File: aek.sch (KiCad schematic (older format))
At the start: 223 parts, among them J1 Conn_01x04_MountingPin, SW1 SW_Push, U1 ATmega32U4-AU, Y1 16MHz

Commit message: updates
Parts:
- added H1, H2: MountingHole_Pad, MountingHole:MountingHole_2.7mm_M2.5_Pad, symbol Mechanical:MountingHole_Pad
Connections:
- net GND: now also H1.1, H2.1

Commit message: first draft
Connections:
- net COL0: now also U1.32 (PC7); no longer U1.19 (PD1)
- net COL1: now also U1.31 (PC6); no longer U1.20 (PD2)
- net COL2: now also U1.30 (PB6); no longer U1.21 (PD3)
- net COL3: now also U1.29 (PB5); no longer U1.25 (PD4)
- net COL4: now also U1.28 (PB4); no longer U1.22 (PD5)
- net COL5: now also U1.27 (PD7); no longer U1.26 (PD6)
- net COL6: now also U1.26 (PD6); no longer U1.27 (PD7)
- net COL7: now also U1.25 (PD4); no longer U1.41 (PF0)
- net COL8: now also U1.21 (PD3); no longer U1.40 (PF1)
- net COL9: now also U1.8 (PB0); no longer U1.39 (PF4)
- net ROW0: now also U1.22 (PD5); no longer D100.1 (K), U1.8 (PB0)
- net ROW1: now also U1.37 (PF6); no longer U1.9 (PB1)
- net ROW10: now also D100.1 (K), U1.38 (PF5); no longer D110.1 (K), U1.18 (PD0)
- net ROW2: now also U1.9 (PB1); no longer U1.10 (PB2)
- net ROW3: now also D103.1 (K), D15.1 (K), D26.1 (K), D37.1 (K), D4.1 (K), D48.1 (K), D59.1 (K), D70.1 (K), D81.1 (K), D92.1 (K)
- net ROW4: now also U1.18 (PD0); no longer U1.28 (PB4)
- net ROW5: now also U1.20 (PD2); no longer U1.29 (PB5)
- net ROW6: now also U1.19 (PD1); no longer U1.30 (PB6)
- net ROW8: now also D109.1 (K), U1.10 (PB2); no longer U1.31 (PC6)
- net ROW9: now also D110.1 (K), U1.36 (PF7); no longer D109.1 (K), U1.32 (PC7)
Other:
- moved on the sheet: D100, D109, D110, SW_KPASTR1, SW_KPMINUS1, SW_POW1
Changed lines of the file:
@@
 Wire Wire Line
 	8200 7500 8200 9000
-Connection ~ 12350 1500
 Connection ~ 11650 1500
 Connection ~ 10950 1500
@@
 Connection ~ 6850 1500
 Wire Wire Line
-	12350 1500 12350 1150
-Wire Wire Line
-	12350 1500 12350 2250
-Wire Wire Line
 	11650 1500 11650 1150
 Wire Wire Line
@@
 ROW0
 Wire Wire Line
-	12050 9200 12150 9200
+	12050 8450 12150 8450
 $Comp
 L Device:D_Small D110
 U 1 1 6145A318
-P 12050 9300
-F 0 "D110" V 12096 9230 50  0000 R CNN
-F 1 "D_Small" V 12005 9230 50  0000 R CNN
-F 2 "Diode_SMD:D_SOD-123" V 12050 9300 50  0001 C CNN
-F 3 "~" V 12050 9300 50  0001 C CNN
-	1    12050 9300
+P 12050 8550
+F 0 "D110" V 12096 8480 50  0000 R CNN
+F 1 "D_Small" V 12005 8480 50  0000 R CNN
+F 2 "Diode_SMD:D_SOD-123" V 12050 8550 50  0001 C CNN
+F 3 "~" V 12050 8550 50  0001 C CNN
+	1    12050 8550
 	0    -1   -1   0
 $EndComp
@@
 Wire Wire Line
 	10650 9400 11350 9400
-Connection ~ 11350 9400
 Wire Wire Line
-	11350 9400 12050 9400
+	11350 8650 12050 8650
 Connection ~ 8600 9400
 Connection ~ 7200 9400
@@
 Wire Wire Line
 	11650 9000 11650 8250
-Wire Wire Line
-	12350 8250 12350 9000
 Connection ~ 6150 8250
 Connection ~ 6850 8250
@@
 Connection ~ 10950 8250
 Connection ~ 11650 8250
-Connection ~ 12350 8250
-Wire Wire Line
-	11350 1900 12050 1900
 Wire Wire Line
 	11350 2650 12050 2650
@@
 	11350 4900 12050 4900
 Wire Wire Line
-	11350 8650 12050 8650
-Connection ~ 11350 8650
+	11350 7900 12050 7900
 Connection ~ 11350 4900
 Connection ~ 11350 4150
 Connection ~ 11350 3400
 Connection ~ 11350 2650
-Connection ~ 11350 1900
 Wire Wire Line
 	6850 2250 6850 3000
@@
 L Device:D_Small D109
 U 1 1 6145A285
-P 12050 8550
-F 0 "D109" V 12096 8480 50  0000 R CNN
-F 1 "D_Small" V 12005 8480 50  0000 R CNN
-F 2 "Diode_SMD:D_SOD-123" V 12050 8550 50  0001 C CNN
-F 3 "~" V 12050 8550 50  0001 C CNN
-	1    12050 8550
+P 12050 7800
+F 0 "D109" V 12096 7730 50  0000 R CNN
+F 1 "D_Small" V 12005 7730 50  0000 R CNN
+F 2 "Diode_SMD:D_SOD-123" V 12050 7800 50  0001 C CNN
+F 3 "~" V 12050 7800 50  0001 C CNN
+	1    12050 7800
 	0    -1   -1   0
 $EndComp
 Wire Wire Line
-	12050 8450 12150 8450
+	12050 7700 12150 7700
 Wire Wire Line
 	7900 7700 8000 7700
@@
 Wire Wire Line
 	11350 1700 11450 1700
-$Comp
-L MX_Alps_Hybrid:MX-NoLED SW_POW1
-U 1 1 6126A487
-P 12200 1550
-F 0 "SW_POW1" H 12233 1773 60  0000 C CNN
-F 1 "MX-NoLED" H 12233 1699 20  0000 C CNN
-F 2 "MX_Alps_Hybrid:MX-1U-NoLED" H 11575 1525 60  0001 C CNN
-F 3 "" H 11575 1525 60  0001 C CNN
-	1    12200 1550
-	1    0    0    -1
-$EndComp
-$Comp
-L Device:D_Small D100
-U 1 1 6126A48D
-P 12050 1800
-F 0 "D100" V 12096 1730 50  0000 R CNN
-F 1 "D_Small" V 12005 1730 50  0000 R CNN
-F 2 "Diode_SMD:D_SOD-123" V 12050 1800 50  0001 C CNN
-F 3 "~" V 12050 1800 50  0001 C CNN
-	1    12050 1800
-	0    -1   -1   0
-$EndComp
-Wire Wire Line
-	12050 1700 12150 1700
 Wire Wire Line
 	1200 8750 1200 8950
@@
 L MX_Alps_Hybrid:MX-NoLED SW_KPASTR1
 U 1 1 6145A31E
-P 12200 9050
-F 0 "SW_KPASTR1" H 12233 9273 60  0000 C CNN
-F 1 "MX-NoLED" H 12233 9199 20  0000 C CNN
-F 2 "MX_Alps_Hybrid:MX-1U-NoLED" H 11575 9025 60  0001 C CNN
-F 3 "" H 11575 9025 60  0001 C CNN
-	1    12200 9050
+P 12200 8300
+F 0 "SW_KPASTR1" H 12233 8523 60  0000 C CNN
+F 1 "MX-NoLED" H 12233 8449 20  0000 C CNN
+F 2 "MX_Alps_Hybrid:MX-1U-NoLED" H 11575 8275 60  0001 C CNN
+F 3 "" H 11575 8275 60  0001 C CNN
+	1    12200 8300
 	1    0    0    -1
 $EndComp
 Wire Wire Line
-	12350 4500 12350 8250
+	12350 4500 12350 7500
 $Comp
 L MX_Alps_Hybrid:MX-NoLED SW_KPMINUS1
 U 1 1 6145A28B
-P 12200 8300
-F 0 "SW_KPMINUS1" H 12233 8523 60  0000 C CNN
-F 1 "MX-NoLED" H 12233 8449 20  0000 C CNN
-F 2 "MX_Alps_Hybrid:MX-1U-NoLED" H 11575 8275 60  0001 C CNN
-F 3 "" H 11575 8275 60  0001 C CNN
-	1    12200 8300
+P 12200 7550
+F 0 "SW_KPMINUS1" H 12233 7773 60  0000 C CNN
+F 1 "MX-NoLED" H 12233 7699 20  0000 C CNN
+F 2 "MX_Alps_Hybrid:MX-1U-NoLED" H 11575 7525 60  0001 C CNN
+F 3 "" H 11575 7525 60  0001 C CNN
+	1    12200 7550
 	1    0    0    -1
 $EndComp
@@
 	1    0    0    -1
 $EndComp
-Text GLabel 3150 4700 2    50   Input ~ 0
-ROW7
-Text GLabel 3150 4600 2    50   Input ~ 0
+Text GLabel 3150 5300 2    50   Input ~ 0
 ROW6
-Text GLabel 3150 4500 2    50   Input ~ 0
+Text GLabel 3150 5400 2    50   Input ~ 0
 ROW5
-Text GLabel 3150 4400 2    50   Input ~ 0
+Text GLabel 3150 5200 2    50   Input ~ 0
 ROW4
 Text GLabel 3150 4300 2    50   Input ~ 0
 ROW3
-Text GLabel 3150 4200 2    50   Input ~ 0
-ROW2
 Text GLabel 3150 4100 2    50   Input ~ 0
-ROW1
-Text GLabel 3150 4000 2    50   Input ~ 0
+ROW2
+Text GLabel 3150 5700 2    50   Input ~ 0
 ROW0
-Text GLabel 3150 4900 2    50   Input ~ 0
-ROW8
-Text GLabel 3150 5000 2    50   Input ~ 0
+Text GLabel 3150 6900 2    50   Input ~ 0
 ROW9
-Text GLabel 3150 5200 2    50   Input ~ 0
+Text GLabel 3150 6700 2    50   Input ~ 0
 ROW10
 Text GLabel 6150 1150 1    50   Input ~ 0
@@
 Text GLabel 12350 1150 1    50   Input ~ 0
 COL9
-Text GLabel 3150 6600 2    50   Input ~ 0
+Text GLabel 3150 4000 2    50   Input ~ 0
 COL9
-Text GLabel 3150 6500 2    50   Input ~ 0
+Text GLabel 3150 5500 2    50   Input ~ 0
 COL8
-Text GLabel 3150 6400 2    50   Input ~ 0
+Text GLabel 3150 5600 2    50   Input ~ 0
 COL7
-Text GLabel 3150 5900 2    50   Input ~ 0
-COL6
 Text GLabel 3150 5800 2    50   Input ~ 0
+COL6
+Text GLabel 3150 5900 2    50   Input ~ 0
 COL5
-Text GLabel 3150 5700 2    50   Input ~ 0
+Text GLabel 3150 4400 2    50   Input ~ 0
 COL4
-Text GLabel 3150 5600 2    50   Input ~ 0
+Text GLabel 3150 4500 2    50   Input ~ 0
 COL3
-Text GLabel 3150 5500 2    50   Input ~ 0
+Text GLabel 3150 4600 2    50   Input ~ 0
 COL2
-Text GLabel 3150 5400 2    50   Input ~ 0
+Text GLabel 3150 4900 2    50   Input ~ 0
 COL1
-Text GLabel 3150 5300 2    50   Input ~ 0
+Text GLabel 3150 5000 2    50   Input ~ 0
 COL0
 Wire Wire Line
@@
 	1    0    0    -1
 $EndComp
+Connection ~ 11350 1900
+Wire Wire Line
+	11350 1900 12050 1900
+Wire Wire Line
+	12350 1150 12350 2250
+Connection ~ 11350 7900
+Connection ~ 12350 7500
+Wire Wire Line
+	12350 7500 12350 8250
+Connection ~ 11350 8650
+Connection ~ 12350 8250
+Wire Wire Line
+	12350 8250 12350 9000
+$Comp
+L MX_Alps_Hybrid:MX-NoLED SW_POW1
+U 1 1 6126A487
+P 12200 9050
+F 0 "SW_POW1" H 12233 9273 60  0000 C CNN
+F 1 "MX-NoLED" H 12233 9199 20  0000 C CNN
+F 2 "MX_Alps_Hybrid:MX-1U-NoLED" H 11575 9025 60  0001 C CNN
+F 3 "" H 11575 9025 60  0001 C CNN
+	1    12200 9050
+	1    0    0    -1
+$EndComp
+$Comp
+L Device:D_Small D100
+U 1 1 6126A48D
+P 12050 9300
+F 0 "D100" V 12096 9230 50  0000 R CNN
+F 1 "D_Small" V 12005 9230 50  0000 R CNN
+F 2 "Diode_SMD:D_SOD-123" V 12050 9300 50  0001 C CNN
+F 3 "~" V 12050 9300 50  0001 C CNN
+	1    12050 9300
+	0    -1   -1   0
+$EndComp
+Wire Wire Line
+	12050 9200 12150 9200
+Wire Wire Line
+	12050 9400 11350 9400
+Connection ~ 11350 9400
+Wire Wire Line
+	5800 4150 5850 4150
+Connection ~ 5850 4150
+Wire Wire Line
+	5850 4150 6550 4150
+Text GLabel 3150 6800 2    50   Input ~ 0
+ROW1
+Text GLabel 3150 4200 2    50   Input ~ 0
+ROW8
+Text GLabel 3150 4700 2    50   Input ~ 0
+ROW7
 $EndSCHEMATC

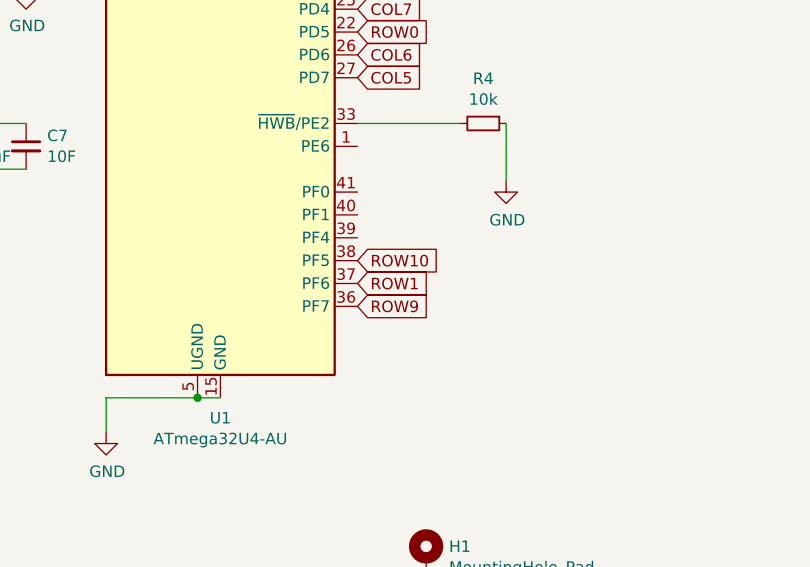
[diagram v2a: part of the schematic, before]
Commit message: reposition mcu
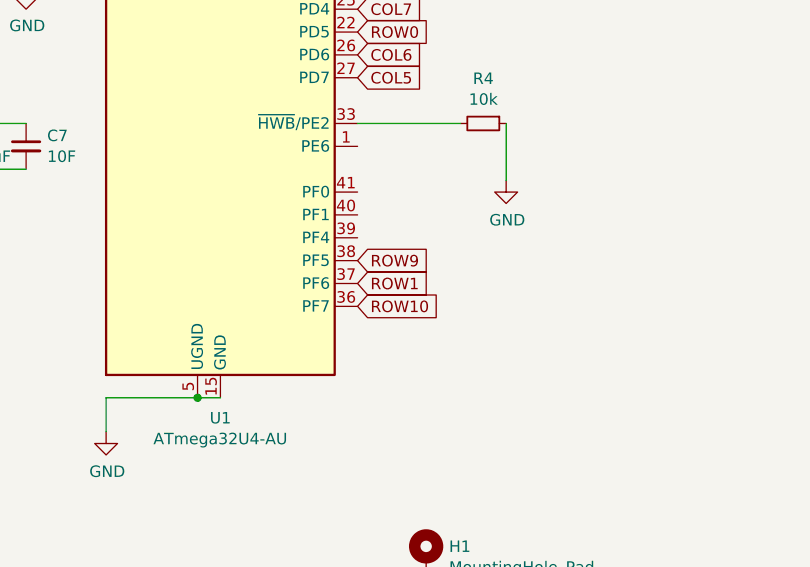
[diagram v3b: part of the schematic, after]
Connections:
- net ROW10: now also U1.36 (PF7); no longer U1.38 (PF5)
- net ROW9: now also U1.38 (PF5); no longer U1.36 (PF7)
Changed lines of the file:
@@
 Text GLabel 3150 5700 2    50   Input ~ 0
 ROW0
-Text GLabel 3150 6900 2    50   Input ~ 0
+Text GLabel 3150 6700 2    50   Input ~ 0
 ROW9
-Text GLabel 3150 6700 2    50   Input ~ 0
-ROW10
 Text GLabel 6150 1150 1    50   Input ~ 0
 COL0
@@
 Text GLabel 3150 4700 2    50   Input ~ 0
 ROW7
+Text GLabel 3150 6900 2    50   Input ~ 0
+ROW10
 $EndSCHEMATC

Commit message: updates
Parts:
- added C10, C8, C9: 0.1uF, Capacitor_SMD:C_0805_2012Metric, symbol Device:C_Small
- added LED1, LED2, LED3: WS2812B, LED_SMD:LED_WS2812B_PLCC4_5.0x5.0mm_P3.2mm, symbol ws2812b:WS2812B
- added R1: 330, Resistor_SMD:R_0805_2012Metric, symbol Device:R_Small
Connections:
- net GND: now also C10.1, C8.1, C9.1, LED1.3 (GND), LED2.3 (GND), LED3.3 (GND)
- net at U1.39 (PF4): now also R1.2
- new net: LED1.4 (DIN), LED2.2 (DOUT)
- new net: LED2.4 (DIN), LED3.2 (DOUT)
- new net LEDDIN: LED3.4 (DIN), R1.1
- new net VCC: C10.2, C8.2, C9.2, LED1.1 (VCC), LED2.1 (VCC), LED3.1 (VCC)
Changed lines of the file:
@@
 L power:GND #PWR0103
 U 1 1 611FF53A
-P 3800 6350
-F 0 "#PWR0103" H 3800 6100 50  0001 C CNN
-F 1 "GND" H 3805 6177 50  0000 C CNN
-F 2 "" H 3800 6350 50  0001 C CNN
-F 3 "" H 3800 6350 50  0001 C CNN
-	1    3800 6350
+P 4450 6100
+F 0 "#PWR0103" H 4450 5850 50  0001 C CNN
+F 1 "GND" H 4455 5927 50  0000 C CNN
+F 2 "" H 4450 6100 50  0001 C CNN
+F 3 "" H 4450 6100 50  0001 C CNN
+	1    4450 6100
 	1    0    0    -1
 $EndComp
@@
 COL0
 Wire Wire Line
-	3800 6100 3800 6350
+	3800 6100 4450 6100
 Connection ~ 7200 3400
 Connection ~ 7200 4150
@@
 	5800 4150 5850 4150
 Connection ~ 5850 4150
-Wire Wire Line
-	5850 4150 6550 4150
 Text GLabel 3150 6800 2    50   Input ~ 0
 ROW1
@@
 Text GLabel 3150 6900 2    50   Input ~ 0
 ROW10
+Text GLabel 3950 6750 2    50   Input ~ 0
+LEDDIN
+$Comp
+L Device:R_Small R1
+U 1 1 6130A8DC
+P 3650 6600
+F 0 "R1" V 3454 6600 50  0000 C CNN
+F 1 "330" V 3545 6600 50  0000 C CNN
+F 2 "Resistor_SMD:R_0805_2012Metric" H 3650 6600 50  0001 C CNN
+F 3 "~" H 3650 6600 50  0001 C CNN
+	1    3650 6600
+	0    1    1    0
+$EndComp
+Wire Wire Line
+	3150 6600 3550 6600
+Wire Wire Line
+	3750 6600 3950 6600
+Wire Wire Line
+	3950 6600 3950 6750
+$Comp
+L power:GND #PWR0115
+U 1 1 6124AC43
+P 3000 13250
+F 0 "#PWR0115" H 3000 13000 50  0001 C CNN
+F 1 "GND" H 3005 13077 50  0000 C CNN
+F 2 "" H 3000 13250 50  0001 C CNN
+F 3 "" H 3000 13250 50  0001 C CNN
+	1    3000 13250
+	1    0    0    -1
+$EndComp
+$Comp
+L ws2812b:WS2812B LED1
+U 1 1 612394E1
+P 4100 11550
+F 0 "LED1" H 4100 12037 60  0000 C CNN
+F 1 "WS2812B" H 4100 11931 60  0000 C CNN
+F 2 "LED_SMD:LED_WS2812B_PLCC4_5.0x5.0mm_P3.2mm" H 4100 11931 60  0001 C CNN
+F 3 "" V 4050 11550 60  0000 C CNN
+	1    4100 11550
+	1    0    0    -1
+$EndComp
+$Comp
+L power:VCC #PWR0116
+U 1 1 61278E0C
+P 5450 10400
+F 0 "#PWR0116" H 5450 10250 50  0001 C CNN
+F 1 "VCC" H 5465 10573 50  0000 C CNN
+F 2 "" H 5450 10400 50  0001 C CNN
+F 3 "" H 5450 10400 50  0001 C CNN
+	1    5450 10400
+	1    0    0    -1
+$EndComp
+$Comp
+L ws2812b:WS2812B LED3
+U 1 1 6197D290
+P 6900 11550
+F 0 "LED3" H 6900 12037 60  0000 C CNN
+F 1 "WS2812B" H 6900 11931 60  0000 C CNN
+F 2 "LED_SMD:LED_WS2812B_PLCC4_5.0x5.0mm_P3.2mm" H 6900 11931 60  0001 C CNN
+F 3 "" V 6850 11550 60  0000 C CNN
+	1    6900 11550
+	1    0    0    -1
+$EndComp
+$Comp
+L ws2812b:WS2812B LED2
+U 1 1 6197B9D3
+P 5500 11550
+F 0 "LED2" H 5500 12037 60  0000 C CNN
+F 1 "WS2812B" H 5500 11931 60  0000 C CNN
+F 2 "LED_SMD:LED_WS2812B_PLCC4_5.0x5.0mm_P3.2mm" H 5500 11931 60  0001 C CNN
+F 3 "" V 5450 11550 60  0000 C CNN
+	1    5500 11550
+	1    0    0    -1
+$EndComp
+$Comp
+L Device:C_Small C8
+U 1 1 6137AF7C
+P 3700 10700
+F 0 "C8" H 3792 10746 50  0000 L CNN
+F 1 "0.1uF" H 3792 10655 50  0000 L CNN
+F 2 "Capacitor_SMD:C_0805_2012Metric" H 3700 10700 50  0001 C CNN
+F 3 "~" H 3700 10700 50  0001 C CNN
+	1    3700 10700
+	0    1    1    0
+$EndComp
+$Comp
+L power:GND #PWR0117
+U 1 1 621F247A
+P 6000 12450
+F 0 "#PWR0117" H 6000 12200 50  0001 C CNN
+F 1 "GND" H 6005 12277 50  0000 C CNN
+F 2 "" H 6000 12450 50  0001 C CNN
+F 3 "" H 6000 12450 50  0001 C CNN
+	1    6000 12450
+	1    0    0    -1
+$EndComp
+$Comp
+L Device:C_Small C10
+U 1 1 62379141
+P 6500 10700
+F 0 "C10" H 6592 10746 50  0000 L CNN
+F 1 "0.1uF" H 6592 10655 50  0000 L CNN
+F 2 "Capacitor_SMD:C_0805_2012Metric" H 6500 10700 50  0001 C CNN
+F 3 "~" H 6500 10700 50  0001 C CNN
+	1    6500 10700
+	0    1    1    0
+$EndComp
+Wire Wire Line
+	6000 11750 6000 12450
+Wire Wire Line
+	4600 11750 4600 12450
+Wire Wire Line
+	5450 10400 5000 10400
+Wire Wire Line
+	3600 10400 3600 10700
+Wire Wire Line
+	5450 10400 6400 10400
+Wire Wire Line
+	6400 10400 6400 10700
+Connection ~ 5450 10400
+Connection ~ 5000 10400
+Wire Wire Line
+	5000 10400 3600 10400
+Text GLabel 7700 11350 2    50   Input ~ 0
+LEDDIN
+Wire Wire Line
+	7700 11350 7400 11350
+Wire Wire Line
+	6400 11750 6400 11550
+Wire Wire Line
+	6400 11550 6000 11550
+Wire Wire Line
+	6000 11550 6000 11350
+Wire Wire Line
+	5000 11750 5000 11550
+Wire Wire Line
+	5000 11550 4600 11550
+Wire Wire Line
+	4600 11550 4600 11350
+Wire Wire Line
+	3600 11750 3350 11750
+Connection ~ 3600 10700
+Wire Wire Line
+	3600 10700 3600 11350
+Connection ~ 6400 10700
+Wire Wire Line
+	6400 10700 6400 11350
+Wire Wire Line
+	7400 11750 7400 12450
+$Comp
+L power:GND #PWR0118
+U 1 1 62D43C91
+P 4050 10700
+F 0 "#PWR0118" H 4050 10450 50  0001 C CNN
+F 1 "GND" H 4055 10527 50  0000 C CNN
+F 2 "" H 4050 10700 50  0001 C CNN
+F 3 "" H 4050 10700 50  0001 C CNN
+	1    4050 10700
+	0    -1   -1   0
+$EndComp
+Wire Wire Line
+	3800 10700 4050 10700
+$Comp
+L power:GND #PWR0119
+U 1 1 62D7BD9A
+P 4600 12450
+F 0 "#PWR0119" H 4600 12200 50  0001 C CNN
+F 1 "GND" H 4605 12277 50  0000 C CNN
+F 2 "" H 4600 12450 50  0001 C CNN
+F 3 "" H 4600 12450 50  0001 C CNN
+	1    4600 12450
+	1    0    0    -1
+$EndComp
+$Comp
+L power:GND #PWR0120
+U 1 1 62D83277
+P 7400 12450
+F 0 "#PWR0120" H 7400 12200 50  0001 C CNN
+F 1 "GND" H 7405 12277 50  0000 C CNN
+F 2 "" H 7400 12450 50  0001 C CNN
+F 3 "" H 7400 12450 50  0001 C CNN
+	1    7400 12450
+	1    0    0    -1
+$EndComp
+$Comp
+L power:GND #PWR0121
+U 1 1 62D839C5
+P 6800 10700
+F 0 "#PWR0121" H 6800 10450 50  0001 C CNN
+F 1 "GND" H 6805 10527 50  0000 C CNN
+F 2 "" H 6800 10700 50  0001 C CNN
+F 3 "" H 6800 10700 50  0001 C CNN
+	1    6800 10700
+	0    -1   -1   0
+$EndComp
+Wire Wire Line
+	5000 10400 5000 10700
+Connection ~ 5000 10700
+Wire Wire Line
+	5000 10700 5000 11350
+$Comp
+L Device:C_Small C9
+U 1 1 621325ED
+P 5100 10700
+F 0 "C9" H 5192 10746 50  0000 L CNN
+F 1 "0.1uF" H 5192 10655 50  0000 L CNN
+F 2 "Capacitor_SMD:C_0805_2012Metric" H 5100 10700 50  0001 C CNN
+F 3 "~" H 5100 10700 50  0001 C CNN
+	1    5100 10700
+	0    1    1    0
+$EndComp
+$Comp
+L power:GND #PWR0122
+U 1 1 62D7FA27
+P 5400 10700
+F 0 "#PWR0122" H 5400 10450 50  0001 C CNN
+F 1 "GND" H 5405 10527 50  0000 C CNN
+F 2 "" H 5400 10700 50  0001 C CNN
+F 3 "" H 5400 10700 50  0001 C CNN
+	1    5400 10700
+	0    -1   -1   0
+$EndComp
+Wire Wire Line
+	5200 10700 5400 10700
+Wire Wire Line
+	6600 10700 6800 10700
 $EndSCHEMATC

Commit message: update
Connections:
- net VCC is gone; now on net +5V: C10.2, C8.2, C9.2, LED1.1 (VCC), LED2.1 (VCC), LED3.1 (VCC)
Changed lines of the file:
@@
-$EndComp
-$Comp
-L power:VCC #PWR0116
-U 1 1 61278E0C
-P 5450 10400
-F 0 "#PWR0116" H 5450 10250 50  0001 C CNN
-F 1 "VCC" H 5465 10573 50  0000 C CNN
-F 2 "" H 5450 10400 50  0001 C CNN
-F 3 "" H 5450 10400 50  0001 C CNN
-	1    5450 10400
-	1    0    0    -1
 $EndComp
 $Comp
@@
 	4600 11750 4600 12450
 Wire Wire Line
-	5450 10400 5000 10400
-Wire Wire Line
 	3600 10400 3600 10700
 Wire Wire Line
-	5450 10400 6400 10400
-Wire Wire Line
 	6400 10400 6400 10700
-Connection ~ 5450 10400
 Connection ~ 5000 10400
 Wire Wire Line
@@
 Wire Wire Line
 	6600 10700 6800 10700
+Wire Wire Line
+	5000 10400 6400 10400
+$Comp
+L power:+5V #PWR?
+U 1 1 62F02BA2
+P 5000 10250
+F 0 "#PWR?" H 5000 10100 50  0001 C CNN
+F 1 "+5V" H 5015 10423 50  0000 C CNN
+F 2 "" H 5000 10250 50  0001 C CNN
+F 3 "" H 5000 10250 50  0001 C CNN
+	1    5000 10250
+	1    0    0    -1
+$EndComp
+Wire Wire Line
+	5000 10250 5000 10400
 $EndSCHEMATC

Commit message: update
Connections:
- net +5V: no longer C10.2, C8.2, C9.2, LED1.1 (VCC), LED2.1 (VCC), LED3.1 (VCC)
- net COL0: now also U1.38 (PF5); no longer U1.32 (PC7)
- net COL1: now also U1.37 (PF6); no longer U1.31 (PC6)
- net COL2: now also U1.36 (PF7); no longer U1.30 (PB6)
- net COL3: now also U1.32 (PC7); no longer U1.29 (PB5)
- net COL4: now also U1.31 (PC6); no longer U1.28 (PB4)
- net COL5: now also U1.30 (PB6); no longer U1.27 (PD7)
- net COL6: now also U1.29 (PB5); no longer U1.26 (PD6)
- net COL7: now also U1.28 (PB4); no longer U1.25 (PD4)
- net COL8: now also U1.26 (PD6); no longer U1.21 (PD3)
- net ROW0: now also U1.27 (PD7); no longer U1.22 (PD5)
- net ROW1: now also U1.18 (PD0); no longer U1.37 (PF6)
- net ROW10: now also U1.20 (PD2); no longer U1.36 (PF7)
- net ROW4: now also U1.21 (PD3); no longer U1.18 (PD0)
- net ROW5: now also U1.25 (PD4); no longer U1.20 (PD2)
- net ROW6: now also U1.22 (PD5); no longer U1.19 (PD1)
- net ROW9: now also U1.19 (PD1); no longer U1.38 (PF5)
- new net: C10.2, C8.2, C9.2, LED1.1 (VCC), LED2.1 (VCC), LED3.1 (VCC)
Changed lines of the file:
@@
 	1    0    0    -1
 $EndComp
-Text GLabel 3150 5300 2    50   Input ~ 0
+Text GLabel 3150 5700 2    50   Input ~ 0
 ROW6
-Text GLabel 3150 5400 2    50   Input ~ 0
+Text GLabel 3150 5600 2    50   Input ~ 0
 ROW5
-Text GLabel 3150 5200 2    50   Input ~ 0
+Text GLabel 3150 5500 2    50   Input ~ 0
 ROW4
 Text GLabel 3150 4300 2    50   Input ~ 0
@@
 Text GLabel 3150 4100 2    50   Input ~ 0
 ROW2
-Text GLabel 3150 5700 2    50   Input ~ 0
+Text GLabel 3150 5900 2    50   Input ~ 0
 ROW0
-Text GLabel 3150 6700 2    50   Input ~ 0
+Text GLabel 3150 5300 2    50   Input ~ 0
 ROW9
 Text GLabel 6150 1150 1    50   Input ~ 0
@@
 Text GLabel 3150 4000 2    50   Input ~ 0
 COL9
-Text GLabel 3150 5500 2    50   Input ~ 0
+Text GLabel 3150 5800 2    50   Input ~ 0
 COL8
-Text GLabel 3150 5600 2    50   Input ~ 0
+Text GLabel 3150 4400 2    50   Input ~ 0
 COL7
-Text GLabel 3150 5800 2    50   Input ~ 0
-COL6
-Text GLabel 3150 5900 2    50   Input ~ 0
+Text GLabel 3150 4600 2    50   Input ~ 0
 COL5
-Text GLabel 3150 4400 2    50   Input ~ 0
+Text GLabel 3150 4900 2    50   Input ~ 0
 COL4
-Text GLabel 3150 4500 2    50   Input ~ 0
+Text GLabel 3150 5000 2    50   Input ~ 0
 COL3
-Text GLabel 3150 4600 2    50   Input ~ 0
+Text GLabel 3150 6900 2    50   Input ~ 0
 COL2
-Text GLabel 3150 4900 2    50   Input ~ 0
+Text GLabel 3150 6800 2    50   Input ~ 0
 COL1
-Text GLabel 3150 5000 2    50   Input ~ 0
+Text GLabel 3150 6700 2    50   Input ~ 0
 COL0
 Wire Wire Line
@@
 	5800 4150 5850 4150
 Connection ~ 5850 4150
-Text GLabel 3150 6800 2    50   Input ~ 0
+Text GLabel 3150 5200 2    50   Input ~ 0
 ROW1
 Text GLabel 3150 4200 2    50   Input ~ 0
@@
 Text GLabel 3150 4700 2    50   Input ~ 0
 ROW7
-Text GLabel 3150 6900 2    50   Input ~ 0
+Text GLabel 3150 5400 2    50   Input ~ 0
 ROW10
 Text GLabel 3950 6750 2    50   Input ~ 0
@@
 	5000 10400 6400 10400
 $Comp
-L power:+5V #PWR?
+L power:+5V #PWR0116
 U 1 1 62F02BA2
 P 5000 10250
-F 0 "#PWR?" H 5000 10100 50  0001 C CNN
+F 0 "#PWR0116" H 5000 10100 50  0001 C CNN
 F 1 "+5V" H 5015 10423 50  0000 C CNN
 F 2 "" H 5000 10250 50  0001 C CNN
@@
 	1    0    0    -1
 $EndComp
-Wire Wire Line
-	5000 10250 5000 10400
+Text GLabel 3150 4500 2    50   Input ~ 0
+COL6
 $EndSCHEMATC

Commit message: updates
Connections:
- net +5V: now also C10.2, C8.2, C9.2, LED1.1 (VCC), LED2.1 (VCC), LED3.1 (VCC)
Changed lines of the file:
@@
 Text GLabel 3150 4500 2    50   Input ~ 0
 COL6
+Wire Wire Line
+	5000 10400 5000 10250
 $EndSCHEMATC
